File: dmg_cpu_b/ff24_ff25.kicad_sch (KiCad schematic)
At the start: 44 parts

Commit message: CH1 Regs page completed.
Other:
- company: (none) -> CC-BY-SA-4.0 Régis Galland & Michael Singer -- Derived work from Furrtek
- title: (none) -> DMG CPU B
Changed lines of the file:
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@@
 (kicad_sch (version 20211123) (generator eeschema)
   (paper "A3")
+  (title_block
+    (title "DMG CPU B")
+    (date "2022-03-12")
+    (rev "0")
+    (company "CC-BY-SA-4.0 Régis Galland & Michael Singer -- Derived work from Furrtek")
+    (comment 1 "https://github.com/msinger/dmg-schematics")
+  )
   (junction (at 112.395 159.385) (diameter 0) (color 0 0 0 0)
   )

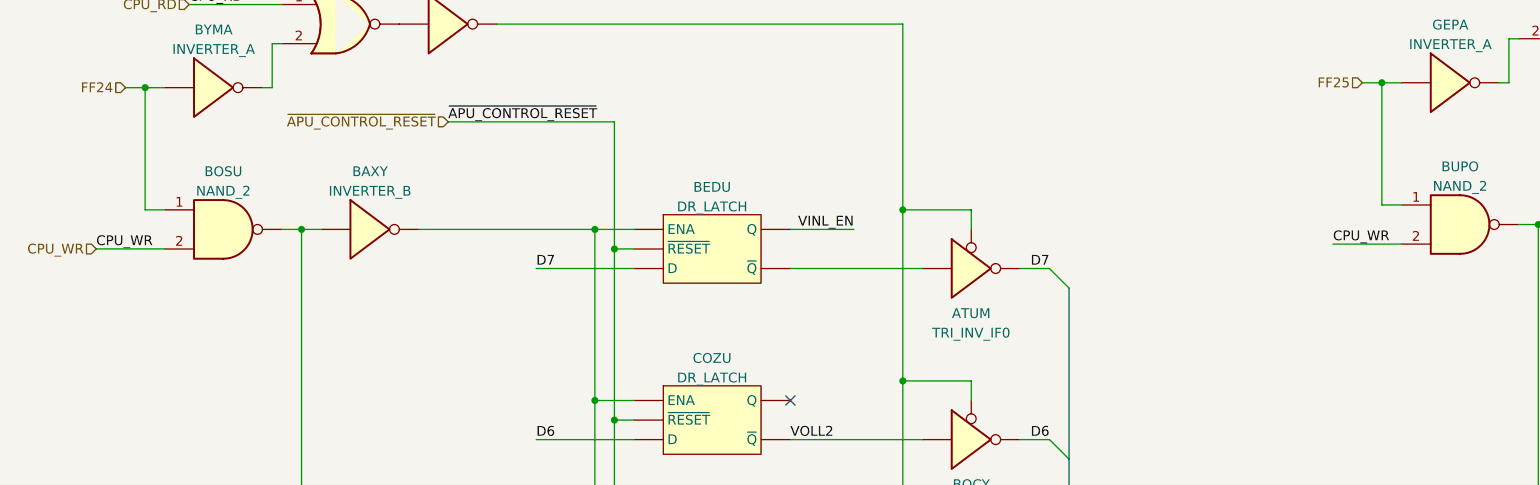
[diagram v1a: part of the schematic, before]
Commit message: CH2 Reg page added.
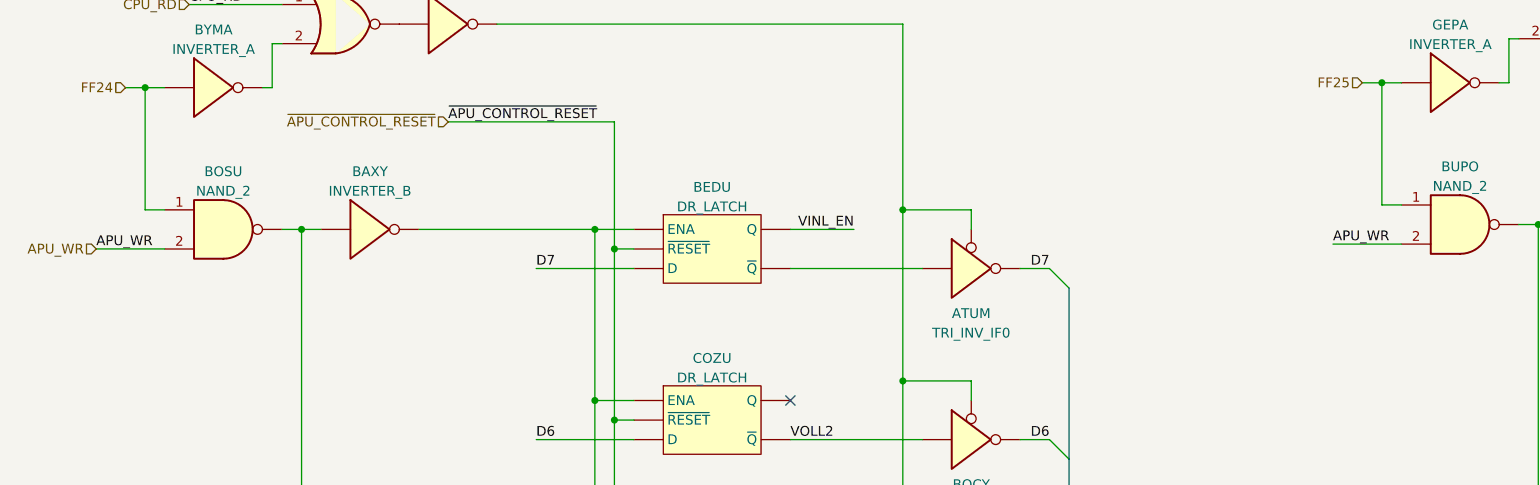
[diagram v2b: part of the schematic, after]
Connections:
- net CPU_WR renamed APU_WR
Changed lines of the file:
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@@
     (effects (font (size 1.27 1.27)) (justify right bottom))
   )
-  (label "CPU_WR" (at 208.28 72.39 0)
+  (label "APU_WR" (at 208.28 72.39 0)
     (effects (font (size 1.27 1.27)) (justify left bottom))
   )
@@
     (effects (font (size 1.27 1.27)) (justify right bottom))
   )
-  (label "CPU_WR" (at 47.625 73.025 0)
+  (label "APU_WR" (at 47.625 73.025 0)
     (effects (font (size 1.27 1.27)) (justify left bottom))
   )
@@
     (effects (font (size 1.27 1.27)) (justify right))
   )
-  (hierarchical_label "CPU_WR" (shape input) (at 47.625 73.025 180)
+  (hierarchical_label "APU_WR" (shape input) (at 47.625 73.025 180)
     (effects (font (size 1.27 1.27)) (justify right))
   )

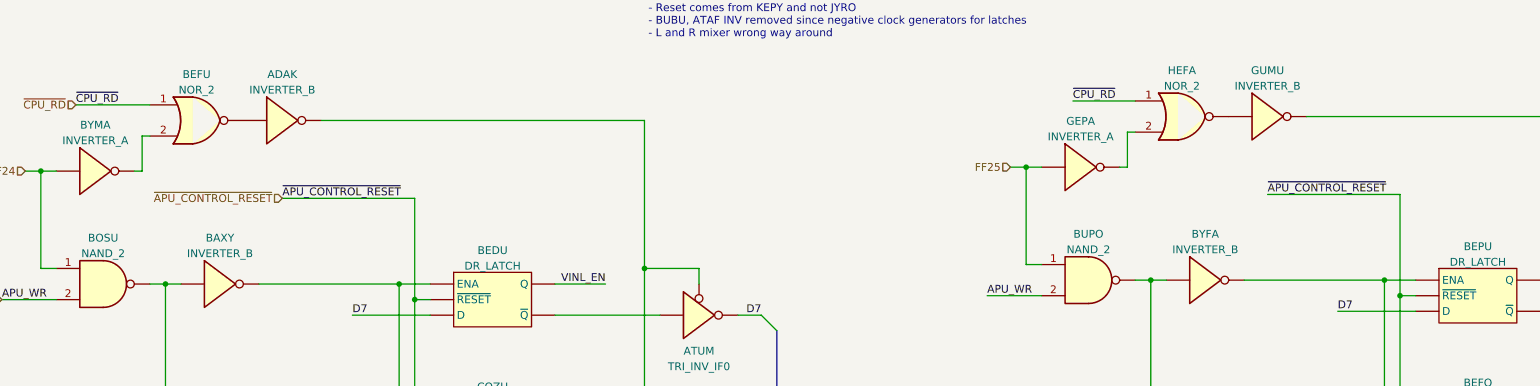
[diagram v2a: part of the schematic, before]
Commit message: fixes made following review
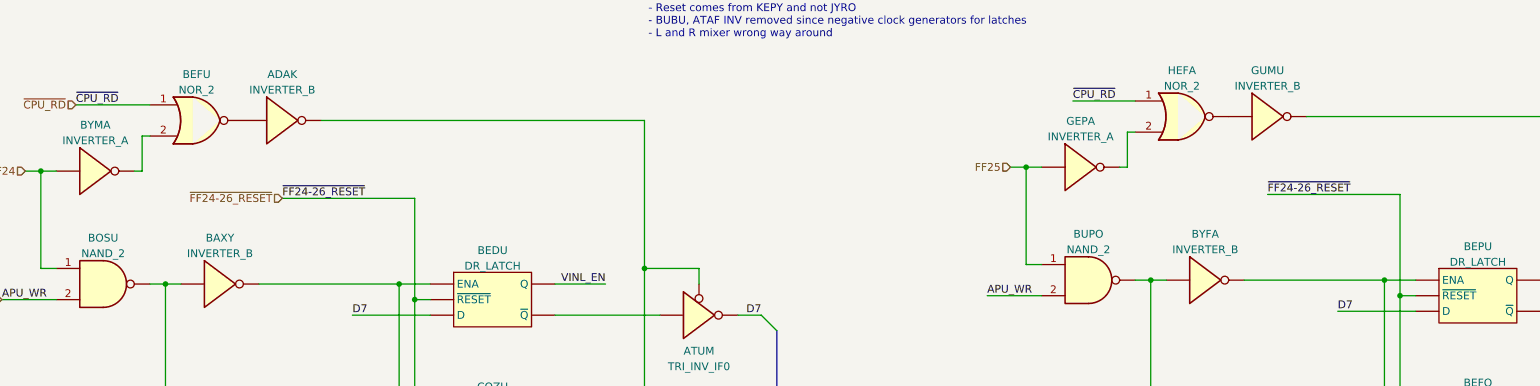
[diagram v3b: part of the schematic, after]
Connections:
- net ~{APU_CONTROL_RESET} renamed ~{FF24-26_RESET}
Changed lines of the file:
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@@
     (effects (font (size 1.27 1.27)) (justify left bottom))
   )
-  (label "~{APU_CONTROL_RESET}" (at 254 55.88 0)
+  (label "~{FF24-26_RESET}" (at 254 55.88 0)
     (effects (font (size 1.27 1.27)) (justify left bottom))
   )
@@
     (effects (font (size 1.27 1.27)) (justify right bottom))
   )
-  (label "~{APU_CONTROL_RESET}" (at 93.345 56.515 0)
+  (label "~{FF24-26_RESET}" (at 93.345 56.515 0)
     (effects (font (size 1.27 1.27)) (justify left bottom))
   )
@@
     (effects (font (size 1.27 1.27)) (justify left bottom))
   )
-  (hierarchical_label "~{APU_CONTROL_RESET}" (shape input) (at 93.345 56.515 180)
+  (hierarchical_label "~{FF24-26_RESET}" (shape input) (at 93.345 56.515 180)
     (effects (font (size 1.27 1.27)) (justify right))
   )

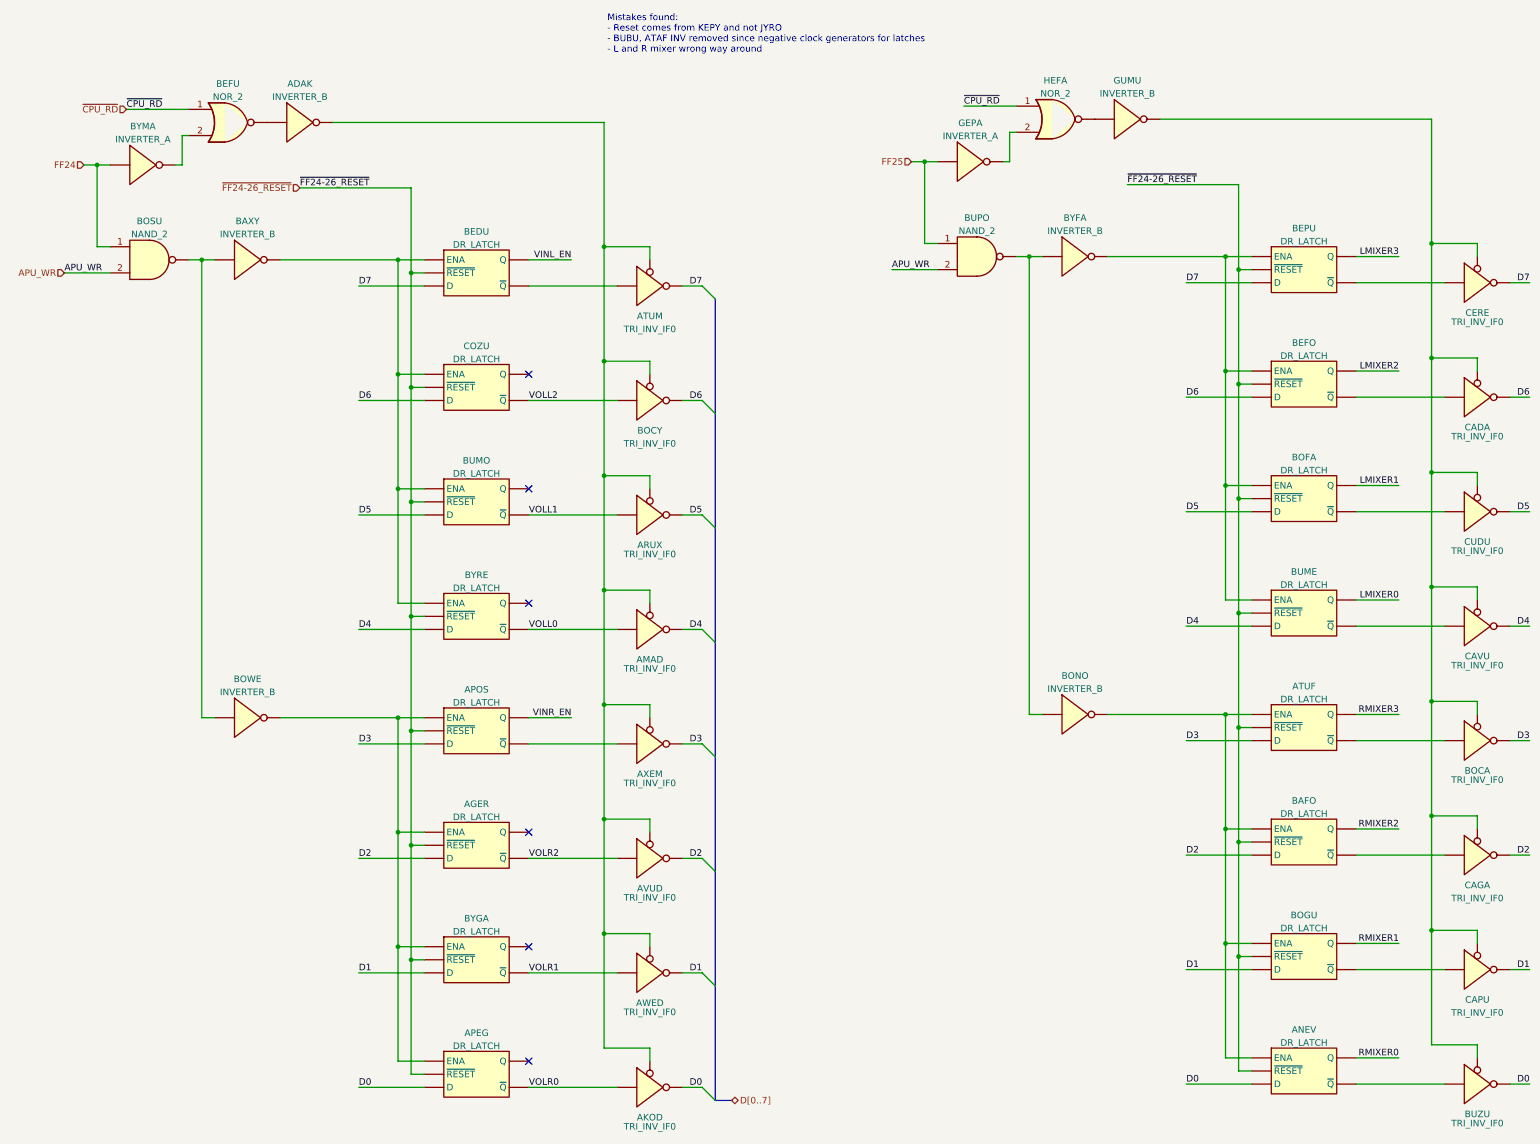
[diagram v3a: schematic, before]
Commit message: Fixes made based on raised issues. PPU decode page added as draft level.
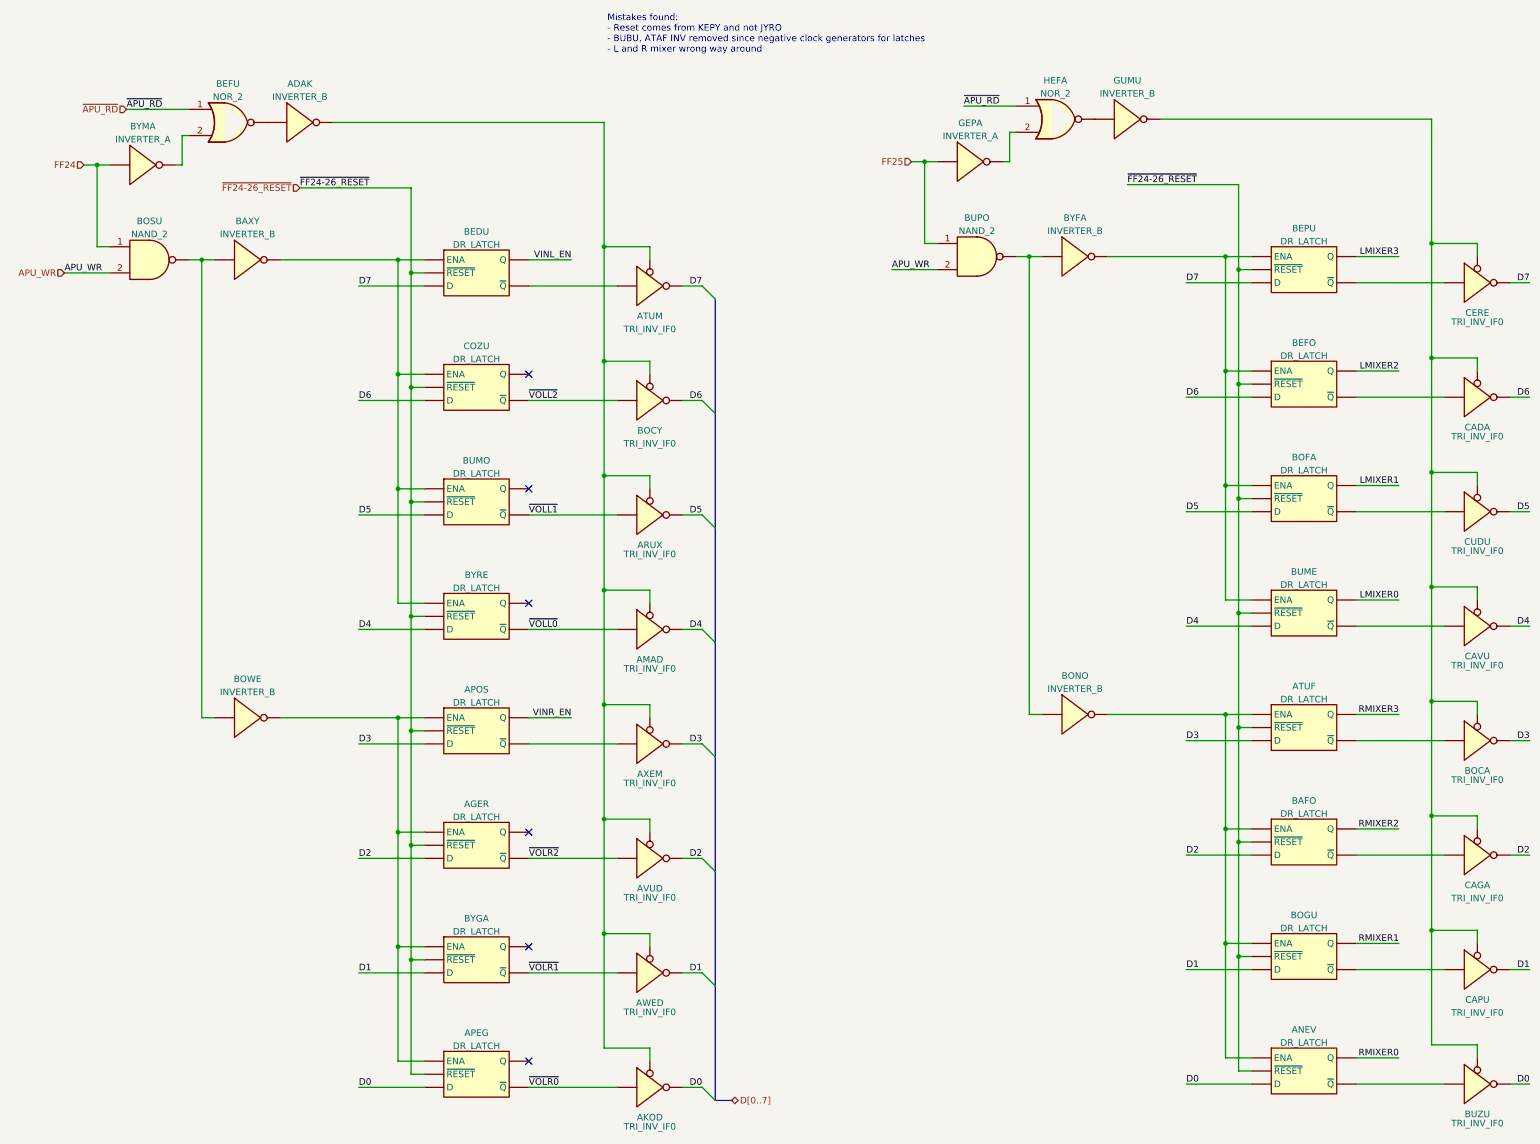
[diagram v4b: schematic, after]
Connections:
- net VOLL0 renamed ~{VOLL0}
- net VOLL1 renamed ~{VOLL1}
- net VOLL2 renamed ~{VOLL2}
- net VOLR0 renamed ~{VOLR0}
- net VOLR1 renamed ~{VOLR1}
- net VOLR2 renamed ~{VOLR2}
- net ~{CPU_RD} renamed ~{APU_RD}
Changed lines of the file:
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@@
     (effects (font (size 1.27 1.27)) (justify right bottom))
   )
-  (label "VOLL2" (at 137.795 97.79 0)
+  (label "~{VOLL2}" (at 137.795 97.79 0)
     (effects (font (size 1.27 1.27)) (justify left bottom))
   )
@@
     (effects (font (size 1.27 1.27)) (justify right bottom))
   )
-  (label "~{CPU_RD}" (at 222.25 40.64 0)
+  (label "~{APU_RD}" (at 222.25 40.64 0)
     (effects (font (size 1.27 1.27)) (justify left bottom))
   )
@@
     (effects (font (size 1.27 1.27)) (justify right bottom))
   )
-  (label "VOLL0" (at 137.795 142.24 0)
+  (label "~{VOLL0}" (at 137.795 142.24 0)
     (effects (font (size 1.27 1.27)) (justify left bottom))
   )
@@
     (effects (font (size 1.27 1.27)) (justify right bottom))
   )
-  (label "VOLR2" (at 137.795 186.69 0)
+  (label "~{VOLR2}" (at 137.795 186.69 0)
     (effects (font (size 1.27 1.27)) (justify left bottom))
   )
@@
     (effects (font (size 1.27 1.27)) (justify left bottom))
   )
-  (label "~{CPU_RD}" (at 59.69 41.275 0)
+  (label "~{APU_RD}" (at 59.69 41.275 0)
     (effects (font (size 1.27 1.27)) (justify left bottom))
   )
@@
     (effects (font (size 1.27 1.27)) (justify right bottom))
   )
-  (label "VOLR0" (at 137.795 231.14 0)
+  (label "~{VOLR0}" (at 137.795 231.14 0)
     (effects (font (size 1.27 1.27)) (justify left bottom))
   )
@@
     (effects (font (size 1.27 1.27)) (justify left bottom))
   )
-  (label "VOLL1" (at 137.795 120.015 0)
+  (label "~{VOLL1}" (at 137.795 120.015 0)
     (effects (font (size 1.27 1.27)) (justify left bottom))
   )
-  (label "VOLR1" (at 137.795 208.915 0)
+  (label "~{VOLR1}" (at 137.795 208.915 0)
     (effects (font (size 1.27 1.27)) (justify left bottom))
   )
@@
     (effects (font (size 1.27 1.27)) (justify left))
   )
-  (hierarchical_label "~{CPU_RD}" (shape input) (at 59.69 41.275 180)
+  (hierarchical_label "~{APU_RD}" (shape input) (at 59.69 41.275 180)
     (effects (font (size 1.27 1.27)) (justify right))
   )

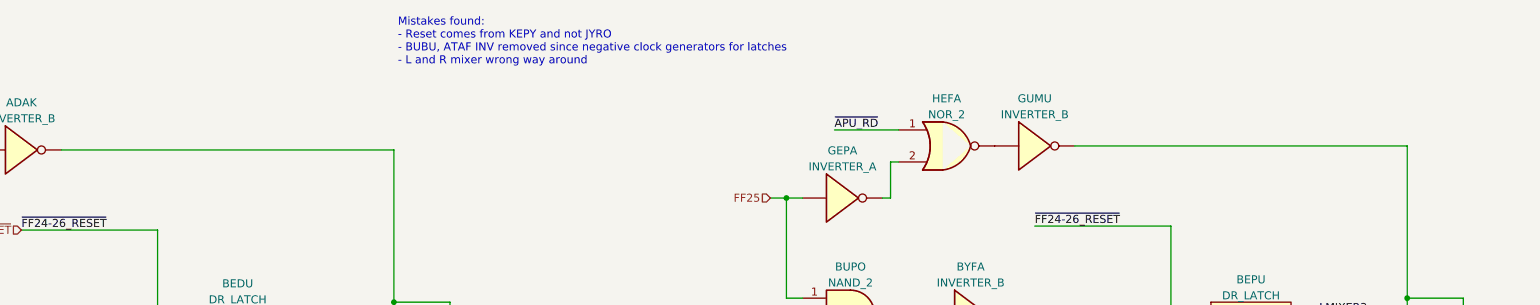
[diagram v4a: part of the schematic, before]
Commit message: VRAM interface sheet added but various edits in existing sheets. Notable merge of RESET, CLOCKS and FF04 DIV sheets
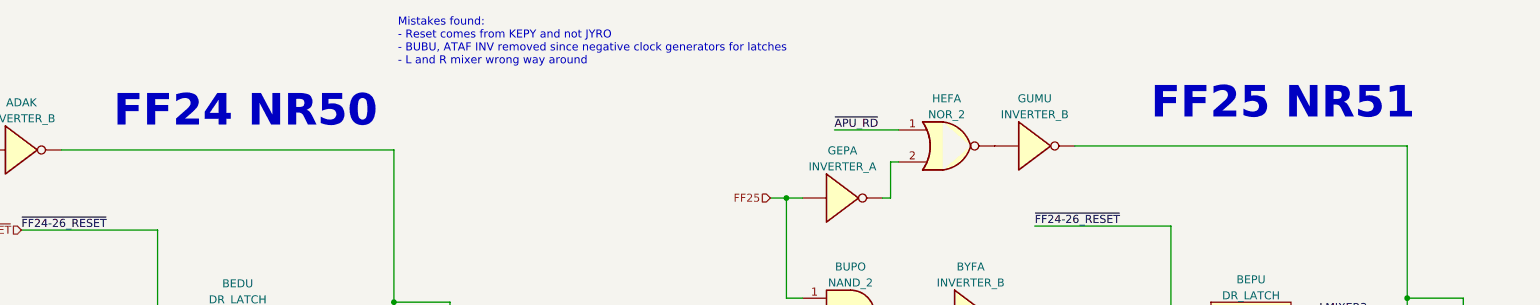
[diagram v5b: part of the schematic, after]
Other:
- note added: "FF24 NR50"
- note added: "FF25 NR51"
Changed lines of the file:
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@@
   (title_block
     (title "DMG CPU B")
-    (date "2022-03-12")
+    (date "2022-05-02")
     (rev "0")
     (company "CC-BY-SA-4.0 Régis Galland & Michael Singer -- Derived work from Furrtek")
@@
     (stroke (width 0) (type default) (color 0 0 0 0))
   )
+  (text "FF24 NR50\n" (at 107.95 40.64 0)
+    (effects (font (size 5 5) (thickness 1) bold) (justify left bottom))
+  )
   (text "Mistakes found: \n- Reset comes from KEPY and not JYRO\n- BUBU, ATAF INV removed since negative clock generators for latches\n- L and R mixer wrong way around"
     (at 153.035 30.48 0)
     (effects (font (size 1.27 1.27)) (justify left bottom))
   )
+  (text "FF25 NR51\n" (at 272.415 39.37 0)
+    (effects (font (size 5 5) (thickness 1) bold) (justify left bottom))
+  )
   (label "RMIXER2" (at 306.705 180.975 180)

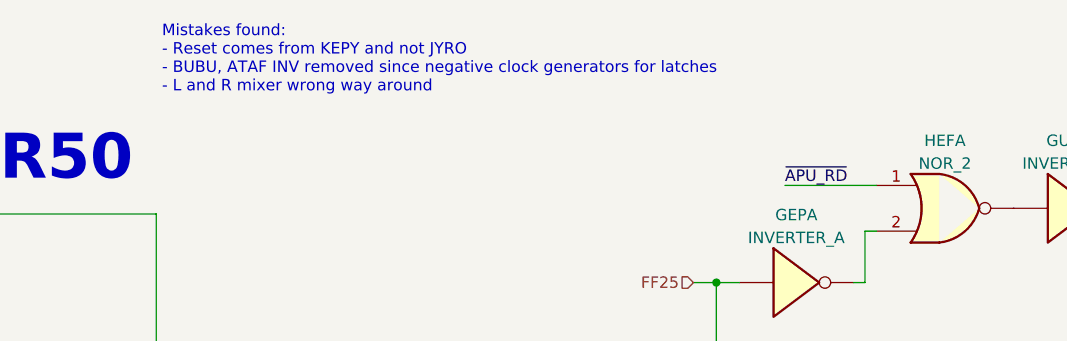
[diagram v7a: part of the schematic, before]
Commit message: Unnecessary comments removed. Data buffers moved to CPU page.
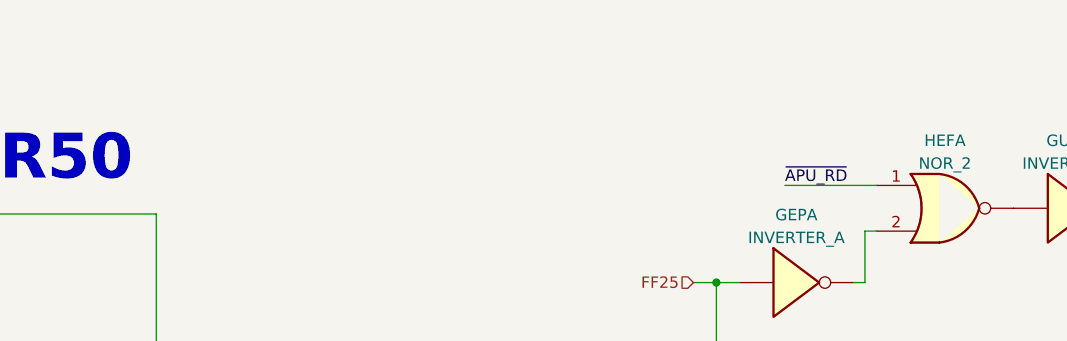
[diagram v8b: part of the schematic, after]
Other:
- note removed: "Mistakes found: - Reset comes from KEPY and not JYRO - BUBU, ATAF INV removed since negative clock generators for latches - L and R mixer wrong way around"
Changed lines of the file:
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@@
     (effects (font (size 5 5) (thickness 1) bold) (justify left bottom))
-  )
-  (text "Mistakes found: \n- Reset comes from KEPY and not JYRO\n- BUBU, ATAF INV removed since negative clock generators for latches\n- L and R mixer wrong way around"
-    (at 153.035 30.48 0)
-    (effects (font (size 1.27 1.27)) (justify left bottom))
   )
   (text "FF25 NR51\n" (at 272.415 39.37 0)
